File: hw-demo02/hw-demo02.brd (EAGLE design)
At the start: 58.4 x 61 mm, 15 parts

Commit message: layout refinement
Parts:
- renumbered TP_VOLTAGE to TP_VDIV
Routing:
- net CTL3`: track 27.1 -> 20.3 mm
- net GND: track 61.8 -> 68.5 mm, vias 21 -> 25
- net +12V: vias 155 -> 152
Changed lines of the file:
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@@
 <layer number="39" name="tKeepout" color="4" fill="11" visible="no" active="yes"/>
 <layer number="40" name="bKeepout" color="1" fill="11" visible="no" active="yes"/>
-<layer number="41" name="tRestrict" color="4" fill="10" visible="no" active="yes"/>
+<layer number="41" name="tRestrict" color="4" fill="10" visible="yes" active="yes"/>
 <layer number="42" name="bRestrict" color="1" fill="10" visible="yes" active="yes"/>
 <layer number="43" name="vRestrict" color="2" fill="10" visible="no" active="yes"/>
@@
 HW-DEMO02</text>
 <text x="49.53" y="58.7375" size="1.27" layer="25" font="vector" ratio="14">GND</text>
-<rectangle x1="50.165" y1="11.7475" x2="50.8" y2="12.065" layer="41"/>
 <rectangle x1="2.2225" y1="17.78" x2="3.175" y2="18.0975" layer="42"/>
+<rectangle x1="45.72" y1="17.4625" x2="47.3075" y2="17.78" layer="41"/>
 </plain>
 <attributes>
@@
 </element>
 <element name="R_GND" library="rcl" package="R1206W" value="0R0" x="33.3375" y="48.26" smashed="yes" rot="R270">
-<attribute name="NAME" x="31.4325" y="52.07" size="0.6096" layer="25" font="vector" ratio="14" rot="R270"/>
+<attribute name="NAME" x="34.6075" y="48.895" size="0.6096" layer="25" font="vector" ratio="14" rot="R270"/>
 </element>
 <element name="Q1" library="BTS500101TADATMA2" package="BTS500101TADATMA2" value="" x="29.5275" y="34.925" smashed="yes" rot="R180">
@@
 </element>
 <element name="C_VS" library="rcl" package="C0805K" value="100n" x="32.7025" y="53.34" smashed="yes" rot="R180">
-<attribute name="NAME" x="32.2325" y="55.23" size="0.6096" layer="25" font="vector" ratio="14" rot="R180"/>
-</element>
-<element name="TP_VOLTAGE" library="con-molex" package="22-23-2021" value="" x="9.525" y="21.59" smashed="yes" rot="R270">
+<attribute name="NAME" x="34.7725" y="55.23" size="0.6096" layer="25" font="vector" ratio="14" rot="R180"/>
+</element>
+<element name="TP_VDIV" library="con-molex" package="22-23-2021" value="" x="9.525" y="21.59" smashed="yes" rot="R270">
 <attribute name="MPN" value="22-23-2021" x="9.525" y="21.59" size="1.778" layer="27" rot="R270" display="off"/>
 <attribute name="MF" value="MOLEX" x="9.525" y="21.59" size="1.778" layer="27" rot="R270" display="off"/>
@@
 <contactref element="LOAD+" pad="1_2"/>
 <contactref element="LOAD+" pad="1_1"/>
-<via x="34.925" y="49.8475" extent="1-16" drill="0.6"/>
-<via x="34.925" y="51.1175" extent="1-16" drill="0.6"/>
+<via x="34.925" y="49.8475" extent="1-16" drill="0.5"/>
+<via x="34.925" y="51.1175" extent="1-16" drill="0.5"/>
 <contactref element="RDIV2" pad="1"/>
 <contactref element="R_ISPD" pad="1"/>
@@
 <contactref element="TP_GND" pad="2"/>
 <contactref element="TP_GND" pad="1"/>
-<wire x1="51.1175" y1="19.05" x2="51.1175" y2="12.3825" width="0.4064" layer="1"/>
-<wire x1="51.1175" y1="12.3825" x2="56.515" y2="6.985" width="0.4064" layer="1"/>
+<wire x1="47.9425" y1="15.5575" x2="56.515" y2="6.985" width="0.4064" layer="1"/>
 <wire x1="56.515" y1="6.985" x2="56.515" y2="5.08" width="0.4064" layer="1"/>
 <wire x1="56.515" y1="5.08" x2="57.785" y2="3.81" width="0.4064" layer="1"/>
-<wire x1="51.1175" y1="19.05" x2="51.1175" y2="21.59" width="0" layer="19" extent="1-1"/>
+<wire x1="47.9425" y1="15.5575" x2="47.9425" y2="18.415" width="0.4064" layer="1"/>
+<wire x1="47.9425" y1="18.415" x2="48.5775" y2="19.05" width="0.4064" layer="1"/>
+<wire x1="48.5775" y1="19.05" x2="51.1175" y2="19.05" width="0.4064" layer="1"/>
+<wire x1="51.1175" y1="19.05" x2="51.1175" y2="21.59" width="0.4064" layer="1"/>
+<via x="30.1625" y="52.705" extent="1-16" drill="0.5"/>
+<via x="30.1625" y="54.2925" extent="1-16" drill="0.5"/>
+<via x="31.4325" y="49.8475" extent="1-16" drill="0.5"/>
+<via x="31.4325" y="51.1175" extent="1-16" drill="0.5"/>
 </signal>
 <signal name="+12V">
@@
 <via x="51.4985" y="6.0325" extent="1-16" drill="0.5"/>
 <via x="57.2897" y="5.715" extent="1-16" drill="0.381"/>
-<via x="46.4185" y="16.8275" extent="1-16" drill="0.5"/>
 <via x="41.021" y="16.8275" extent="1-16" drill="0.5"/>
 <via x="37.5285" y="16.8275" extent="1-16" drill="0.5"/>
@@
 <via x="2.921" y="37.465" extent="1-16" drill="0.5"/>
 <via x="2.921" y="29.5275" extent="1-16" drill="0.5"/>
-<via x="49.911" y="13.0175" extent="1-16" drill="0.5"/>
-<via x="49.911" y="16.8275" extent="1-16" drill="0.5"/>
 </signal>
 <signal name="IN">
@@
 <wire x1="3.81" y1="23.4975" x2="3.81" y2="21.27" width="0.4064" layer="1"/>
 <contactref element="CONTROL" pad="4"/>
-<contactref element="TP_VOLTAGE" pad="1"/>
-<contactref element="TP_VOLTAGE" pad="2"/>
+<contactref element="TP_VDIV" pad="1"/>
+<contactref element="TP_VDIV" pad="2"/>
 <wire x1="9.525" y1="22.86" x2="6.6675" y2="22.86" width="0.4064" layer="1"/>
 <wire x1="6.6675" y1="22.86" x2="6.03" y2="23.4975" width="0.4064" layer="1"/>
@@
 <signal name="CTL3`">
 <contactref element="R_IN" pad="2"/>
-<via x="32.0675" y="48.26" extent="1-16" drill="0.381"/>
-<wire x1="34.6075" y1="47.8109875" x2="34.1584875" y2="48.26" width="0.3048" layer="16"/>
-<wire x1="34.1584875" y1="48.26" x2="32.0675" y2="48.26" width="0.3048" layer="16"/>
+<via x="32.0675" y="44.45" extent="1-16" drill="0.381"/>
 <contactref element="Q1" pad="2"/>
-<wire x1="32.0675" y1="48.26" x2="32.0675" y2="41.35" width="0.4064" layer="1"/>
+<wire x1="32.0675" y1="44.45" x2="32.0675" y2="41.35" width="0.4064" layer="1"/>
 <wire x1="46.0375" y1="38.1" x2="46.0375" y2="39.0525" width="0.3048" layer="16"/>
 <wire x1="46.0375" y1="39.0525" x2="44.45" y2="40.64" width="0.3048" layer="16"/>
 <wire x1="44.45" y1="40.64" x2="39.37" y2="40.64" width="0.3048" layer="16"/>
-<wire x1="39.37" y1="40.64" x2="34.6075" y2="45.4025" width="0.3048" layer="16"/>
-<wire x1="34.6075" y1="47.8109875" x2="34.6075" y2="45.4025" width="0.3048" layer="16"/>
+<wire x1="32.0675" y1="44.45" x2="35.56" y2="44.45" width="0.3048" layer="16"/>
+<wire x1="35.56" y1="44.45" x2="39.37" y2="40.64" width="0.3048" layer="16"/>
 </signal>
 <signal name="IS">

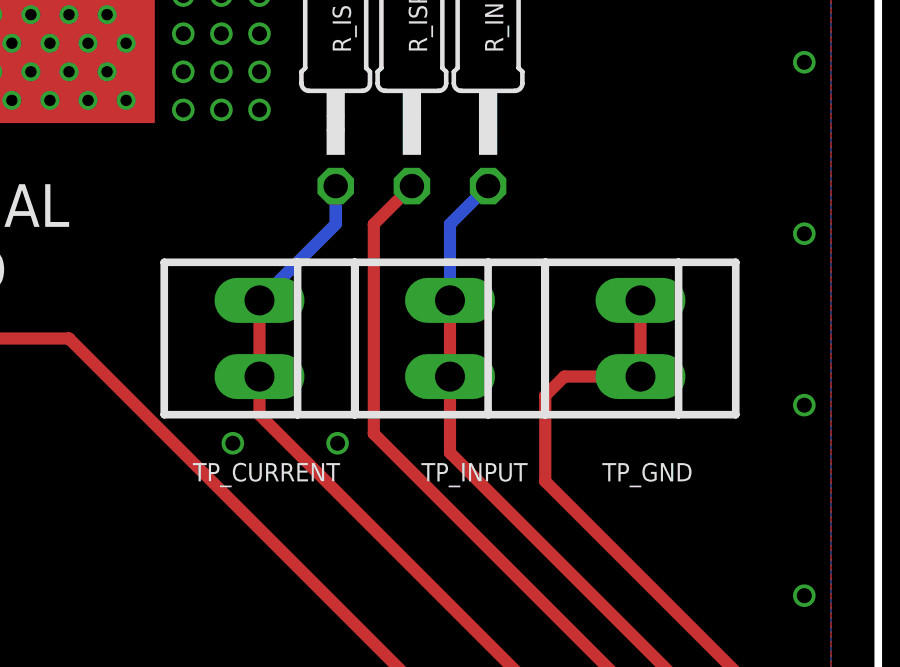
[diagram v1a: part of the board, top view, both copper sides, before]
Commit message: changed layers on some signal routing
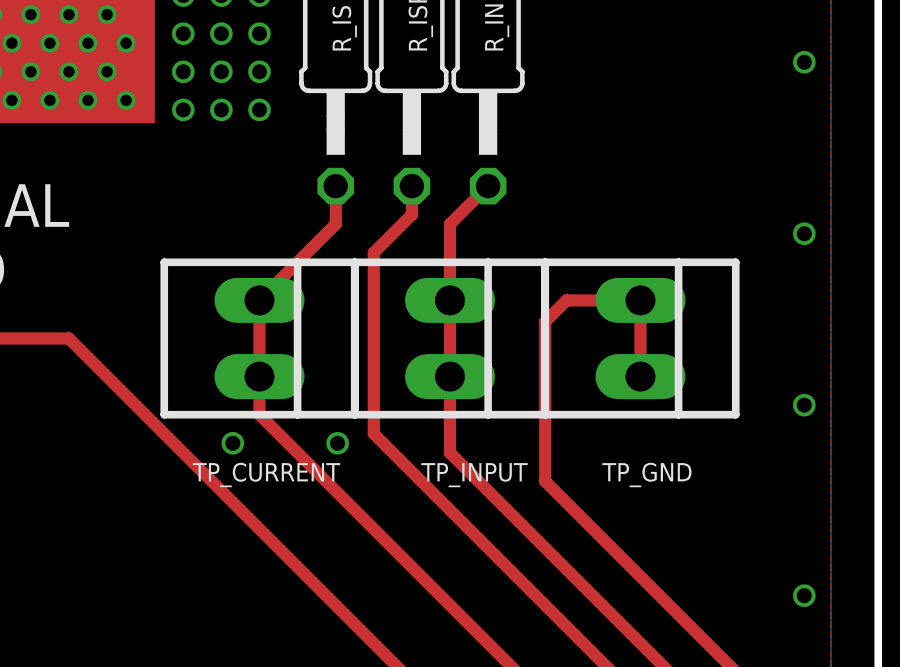
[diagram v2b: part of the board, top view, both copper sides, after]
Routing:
- net GND: track 68.5 -> 70.9 mm
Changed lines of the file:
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@@
 <text x="49.53" y="58.7375" size="1.27" layer="25" font="vector" ratio="14">GND</text>
 <rectangle x1="2.2225" y1="17.78" x2="3.175" y2="18.0975" layer="42"/>
-<rectangle x1="45.72" y1="17.4625" x2="47.3075" y2="17.78" layer="41"/>
+<rectangle x1="46.6725" y1="21.2725" x2="47.625" y2="21.59" layer="41"/>
 </plain>
 <attributes>
@@
 <contactref element="R_GND" pad="1"/>
 <contactref element="C_VS" pad="2"/>
-<wire x1="43.4975" y1="25.4" x2="42.2275" y2="24.13" width="0.4064" layer="1"/>
-<wire x1="42.2275" y1="24.13" x2="42.2275" y2="17.145" width="0.4064" layer="1"/>
+<wire x1="42.2275" y1="23.1775" x2="42.2275" y2="17.145" width="0.4064" layer="1"/>
 <wire x1="42.2275" y1="17.145" x2="52.705" y2="6.6675" width="0.4064" layer="1"/>
 <wire x1="52.705" y1="6.6675" x2="52.705" y2="3.302" width="0.4064" layer="1"/>
@@
 <wire x1="56.515" y1="6.985" x2="56.515" y2="5.08" width="0.4064" layer="1"/>
 <wire x1="56.515" y1="5.08" x2="57.785" y2="3.81" width="0.4064" layer="1"/>
-<wire x1="47.9425" y1="15.5575" x2="47.9425" y2="18.415" width="0.4064" layer="1"/>
-<wire x1="47.9425" y1="18.415" x2="48.5775" y2="19.05" width="0.4064" layer="1"/>
-<wire x1="48.5775" y1="19.05" x2="51.1175" y2="19.05" width="0.4064" layer="1"/>
+<wire x1="47.9425" y1="15.5575" x2="47.9425" y2="20.88005" width="0.4064" layer="1"/>
+<wire x1="47.9425" y1="20.88005" x2="48.65245" y2="21.59" width="0.4064" layer="1"/>
+<wire x1="48.65245" y1="21.59" x2="51.1175" y2="21.59" width="0.4064" layer="1"/>
 <wire x1="51.1175" y1="19.05" x2="51.1175" y2="21.59" width="0.4064" layer="1"/>
 <via x="30.1625" y="52.705" extent="1-16" drill="0.5"/>
@@
 <via x="31.4325" y="49.8475" extent="1-16" drill="0.5"/>
 <via x="31.4325" y="51.1175" extent="1-16" drill="0.5"/>
+<wire x1="42.2275" y1="23.1775" x2="43.4975" y2="24.4475" width="0.4064" layer="1"/>
+<wire x1="43.4975" y1="24.4475" x2="43.4975" y2="25.4" width="0.4064" layer="1"/>
 </signal>
 <signal name="+12V">
@@
 <wire x1="44.7675" y1="21.59" x2="44.7675" y2="19.05" width="0.4064" layer="1"/>
 <wire x1="55.245" y1="3.048" x2="55.245" y2="6.0325" width="0.4064" layer="1"/>
-<wire x1="44.7675" y1="21.59" x2="44.7675" y2="24.13" width="0.4064" layer="16"/>
-<wire x1="44.7675" y1="24.13" x2="46.0375" y2="25.4" width="0.4064" layer="16"/>
+<wire x1="44.7675" y1="21.59" x2="44.7675" y2="24.13" width="0.4064" layer="1"/>
+<wire x1="44.7675" y1="24.13" x2="46.0375" y2="25.4" width="0.4064" layer="1"/>
 <wire x1="55.245" y1="6.0325" x2="44.7675" y2="16.51" width="0.4064" layer="1"/>
 <wire x1="44.7675" y1="16.51" x2="44.7675" y2="19.05" width="0.4064" layer="1"/>
@@
 <wire x1="50.165" y1="3.048" x2="50.165" y2="6.0325" width="0.4064" layer="1"/>
 <wire x1="38.4175" y1="21.59" x2="38.4175" y2="19.05" width="0.4064" layer="1"/>
-<wire x1="38.4175" y1="21.59" x2="40.9575" y2="24.13" width="0.4064" layer="16"/>
-<wire x1="40.9575" y1="24.13" x2="40.9575" y2="25.4" width="0.4064" layer="16"/>
+<wire x1="38.4175" y1="21.59" x2="40.9575" y2="24.13" width="0.4064" layer="1"/>
+<wire x1="40.9575" y1="24.13" x2="40.9575" y2="25.4" width="0.4064" layer="1"/>
 </signal>
 <signal name="N$3">

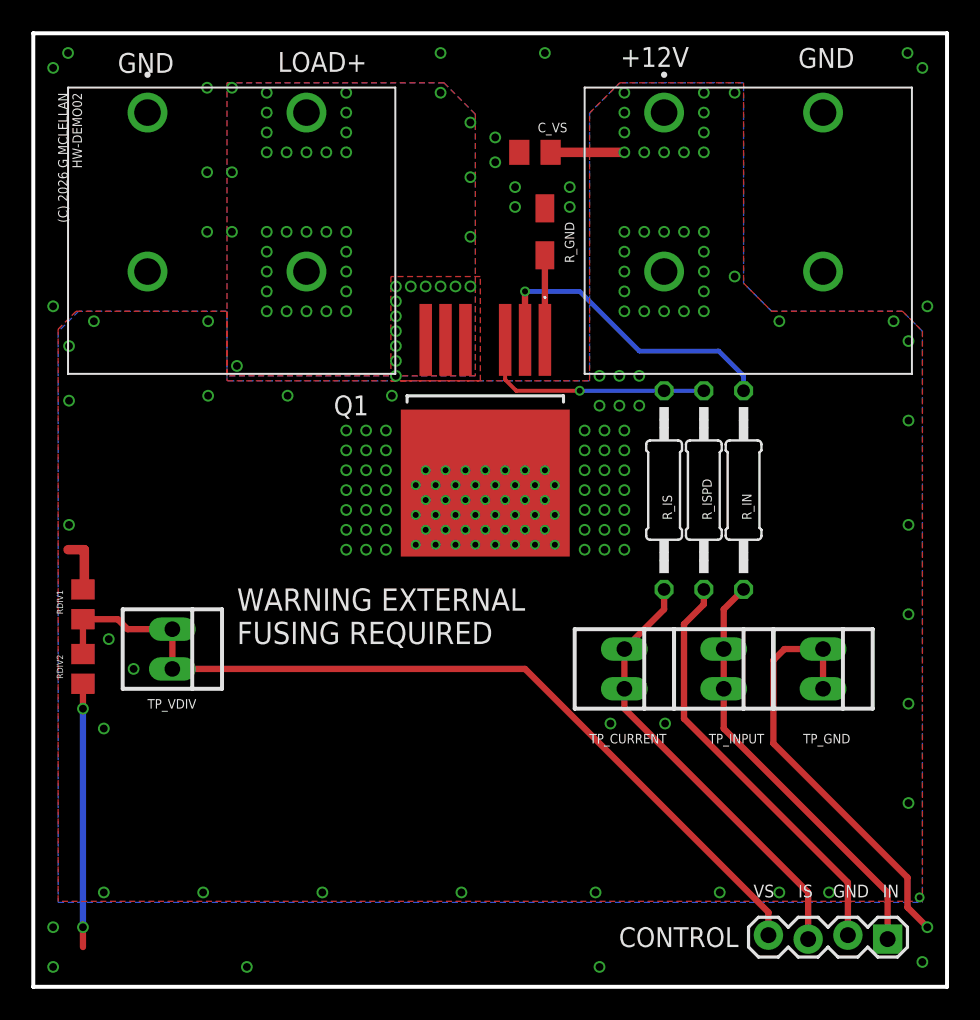
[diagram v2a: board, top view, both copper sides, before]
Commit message: added a lot of stitching based on review of reference designs
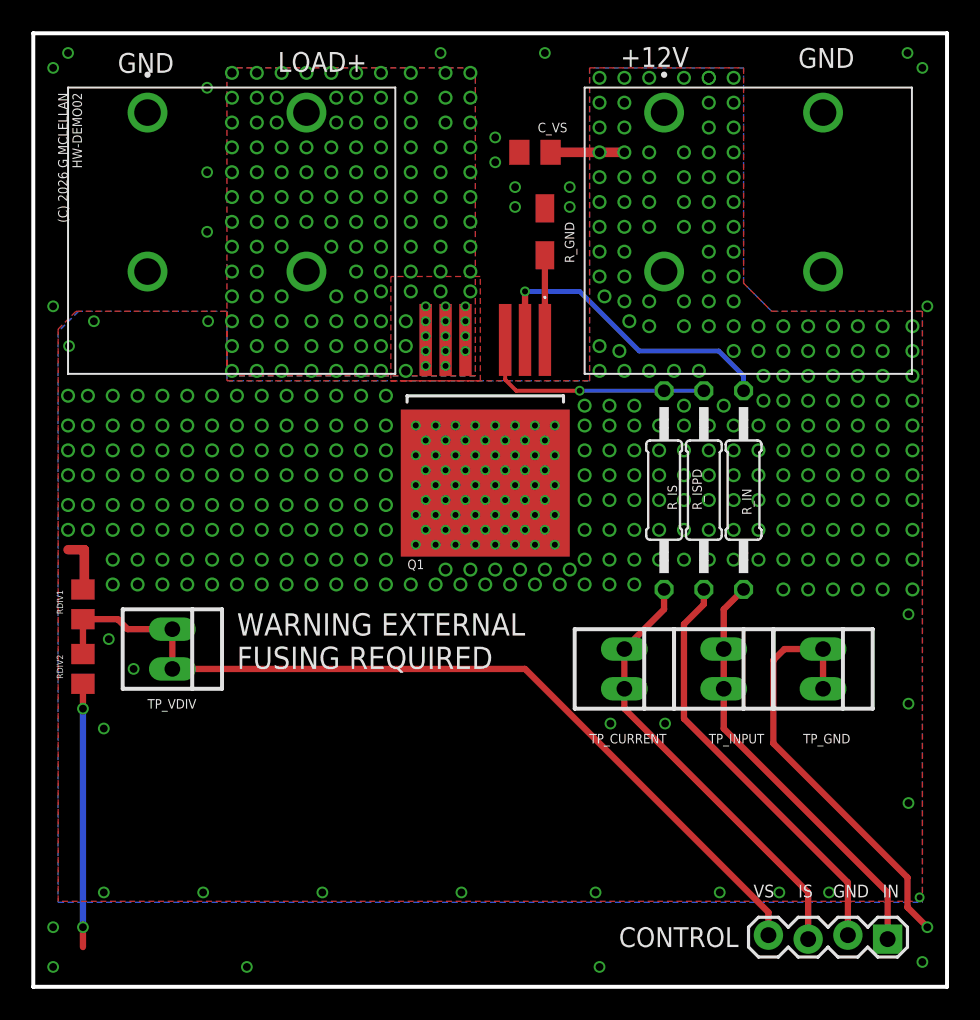
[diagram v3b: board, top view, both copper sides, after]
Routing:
- net +12V: vias 152 -> 401
